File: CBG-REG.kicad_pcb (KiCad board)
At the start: 2 copper layers, 22 x 19.5 mm, 36 parts, among them J1 Conn_01x09_Socket, J2 Conn_01x09_Socket, U1 AD8560ACP-REEL7, U2 AD8560ACP-REEL7, U4 74LVC2G04

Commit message: fix: Update resistor values to those in stock at JLCPCB
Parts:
- R10, R13: value 100k -> 120k
- R11, R14: value 83.5k -> 100k
- R12: value 523k -> 634k
- R15: value 1.15M -> 1.24M
- R16: value 100k -> 107k
- R17: value 92k -> 100k
- R21: value 184k -> 178k
- R22: value 100k -> 95.3k
- R23: value 105k -> 100k
- R24: value 65.7k -> 53.6k
- R25: value 100k -> 80.6k
- R26: value 124k -> 100k
- R27: value 40.7k -> 30k
- R28: value 100k -> 75k
- R29: value 133k -> 100k
- R9: value 240k -> 287k

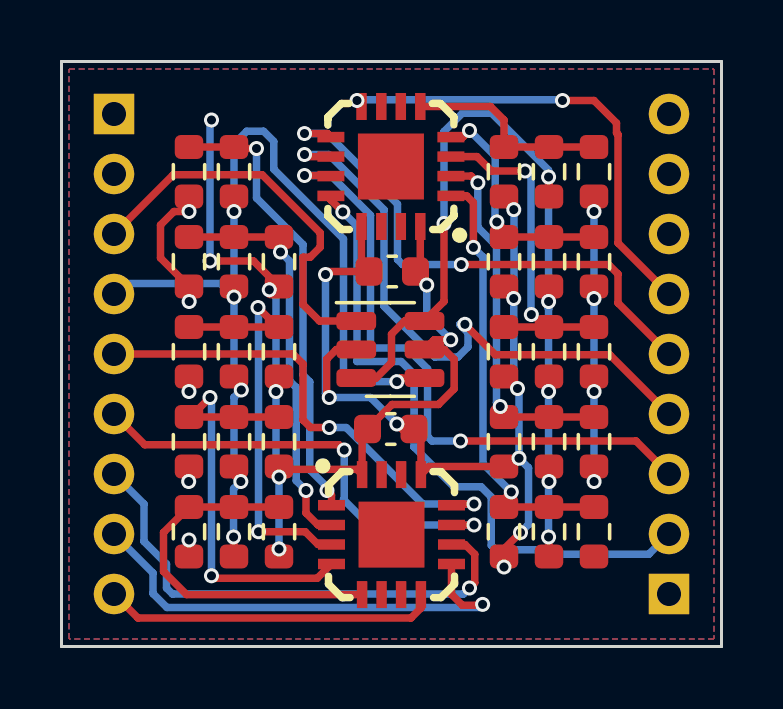
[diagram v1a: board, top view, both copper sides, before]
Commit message: feat: Add PCB silkscreen
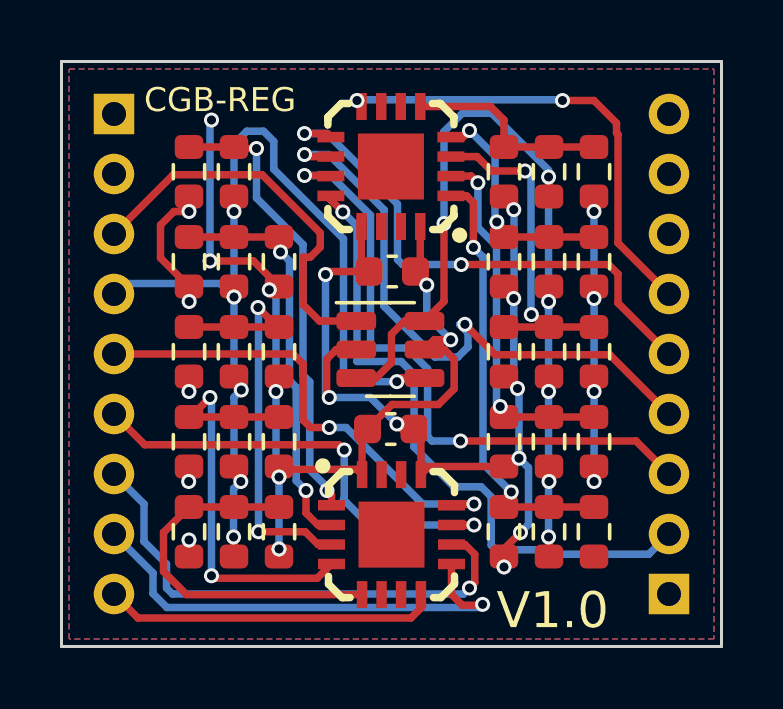
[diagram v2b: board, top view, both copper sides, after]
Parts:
- added G***: LOGO, LOGO, B.Cu at (90.0, 128.2)
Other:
- board text added: "2023"
- board text added: "Broderick Carlin"
- board text added: "CGB-REG"
- board text added: "V1.0"

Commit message: docs: Add pinout to the silkscreen
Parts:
- R17: value 100k -> 97.6k
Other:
- board text added: "Broderick"
- board text added: "COM"
- board text added: "GND"
- board text added: "NC"
- board text added: "SW"
- board text added: "V0"
- board text added: "V1"
- board text added: "V2"
- board text added: "V3"
- board text added: "V4"
- board text added: "V5"
- board text added: "V6"
- board text added: "V7"
- board text added: "V8"
- board text added: "V9"
- board text added: "VCC"
- board text removed: "Broderick Carlin"
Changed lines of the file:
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@@
     (descr "Resistor SMD 0603 (1608 Metric), square (rectangular) end terminal, IPC_7351 nominal, (Body size source: IPC-SM-782 page 72, https://www.pcb-3d.com/wordpress/wp-content/uploads/ipc-sm-782a_amendment_1_and_2.pdf), generated with kicad-footprint-generator")
     (tags "resistor")
-    (property "LCSC" "C414506")
+    (property "LCSC" "C507495")
     (property "Sheetfile" "CBG-REG.kicad_sch")
     (property "Sheetname" "")
@@
         (effects (font (size 1 1) (thickness 0.15)))
     )
-    (fp_text value "100k" (at 0 1.43 90) (layer "F.Fab") hide
+    (fp_text value "97.6k" (at 0 1.43 90) (layer "F.Fab") hide
         (effects (font (size 1 1) (thickness 0.15)))
     )
@@
   (gr_rect (start 79.25 120.75) (end 101.25 140.25)
     (stroke (width 0.1) (type default)) (fill none) (layer "Edge.Cuts"))
-  (gr_text "Broderick Carlin" (at 97.5 137.5) (layer "B.SilkS")
+  (gr_text "V7" (at 98 133.25) (layer "B.SilkS")
+    (effects (font (size 1 1) (thickness 0.15)) (justify left bottom mirror))
+  )
+  (gr_text "SW" (at 84.5 127.25) (layer "B.SilkS")
+    (effects (font (size 1 1) (thickness 0.15)) (justify left bottom mirror))
+  )
+  (gr_text "V9" (at 98 129.25) (layer "B.SilkS")
+    (effects (font (size 1 1) (thickness 0.15)) (justify left bottom mirror))
+  )
+  (gr_text "NC" (at 84.5 123.25) (layer "B.SilkS")
+    (effects (font (size 1 1) (thickness 0.15)) (justify left bottom mirror))
+  )
+  (gr_text "Broderick" (at 94.25 137.75) (layer "B.SilkS")
     (effects (font (size 1.2 1.2) (thickness 0.15)) (justify left bottom mirror))
   )
-  (gr_text "2023" (at 91.75 139.25) (layer "B.SilkS")
-    (effects (font (size 1 1) (thickness 0.15)) (justify left bottom mirror))
-  )
+  (gr_text "2023" (at 92 139.25) (layer "B.SilkS")
+    (effects (font (size 1 1) (thickness 0.15)) (justify left bottom mirror))
+  )
+  (gr_text "V0" (at 84.25 131.25) (layer "B.SilkS")
+    (effects (font (size 1 1) (thickness 0.15)) (justify left bottom mirror))
+  )
+  (gr_text "NC" (at 98 125.25) (layer "B.SilkS")
+    (effects (font (size 1 1) (thickness 0.15)) (justify left bottom mirror))
+  )
+  (gr_text "NC" (at 98 123.25) (layer "B.SilkS")
+    (effects (font (size 1 1) (thickness 0.15)) (justify left bottom mirror))
+  )
+  (gr_text "V8" (at 98 131.25) (layer "B.SilkS")
+    (effects (font (size 1 1) (thickness 0.15)) (justify left bottom mirror))
+  )
+  (gr_text "V6" (at 98 135.25) (layer "B.SilkS")
+    (effects (font (size 1 1) (thickness 0.15)) (justify left bottom mirror))
+  )
+  (gr_text "V3" (at 84.25 137.25) (layer "B.SilkS")
+    (effects (font (size 1 1) (thickness 0.15)) (justify left bottom mirror))
+  )
+  (gr_text "V2" (at 84.25 135.25) (layer "B.SilkS")
+    (effects (font (size 1 1) (thickness 0.15)) (justify left bottom mirror))
+  )
+  (gr_text "V4" (at 84.25 139.25) (layer "B.SilkS")
+    (effects (font (size 1 1) (thickness 0.15)) (justify left bottom mirror))
+  )
+  (gr_text "GND" (at 98.25 139.25) (layer "B.SilkS")
+    (effects (font (size 1 1) (thickness 0.15)) (justify left bottom mirror))
+  )
+  (gr_text "V1" (at 84.25 133.25) (layer "B.SilkS")
+    (effects (font (size 1 1) (thickness 0.15)) (justify left bottom mirror))
+  )
+  (gr_text "V5" (at 98 137.25) (layer "B.SilkS")
+    (effects (font (size 1 1) (thickness 0.15)) (justify left bottom mirror))
+  )
+  (gr_text "COM" (at 85.5 129.25) (layer "B.SilkS")
+    (effects (font (size 1 1) (thickness 0.15)) (justify left bottom mirror))
+  )
+  (gr_text "VCC" (at 98 127.25) (layer "B.SilkS")
+    (effects (font (size 1 1) (thickness 0.15)) (justify left bottom mirror))
+  )
+  (gr_text "NC" (at 84.5 125.25) (layer "B.SilkS")
+    (effects (font (size 1 1) (thickness 0.15)) (justify left bottom mirror))
+  )

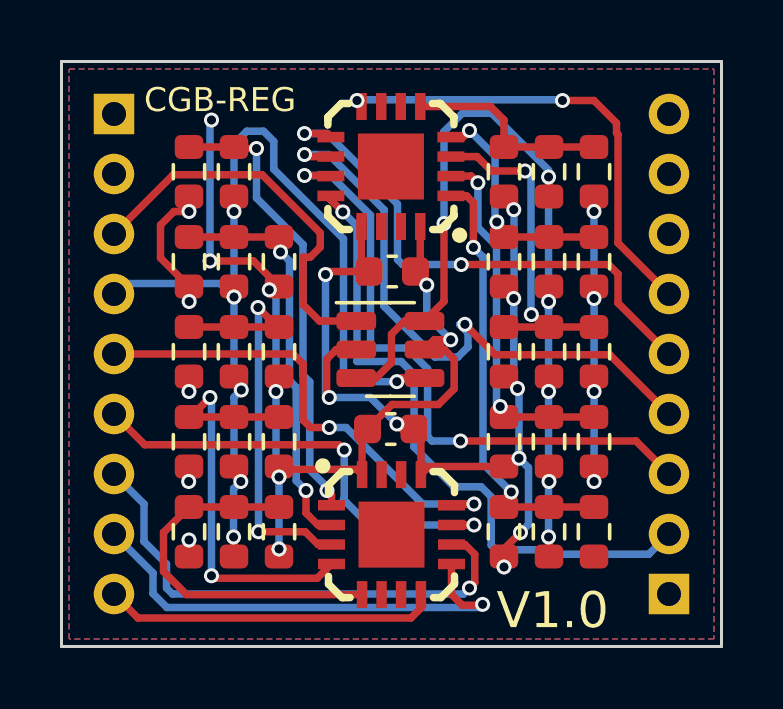
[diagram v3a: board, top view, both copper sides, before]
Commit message: feat: Switch connector to use castellations
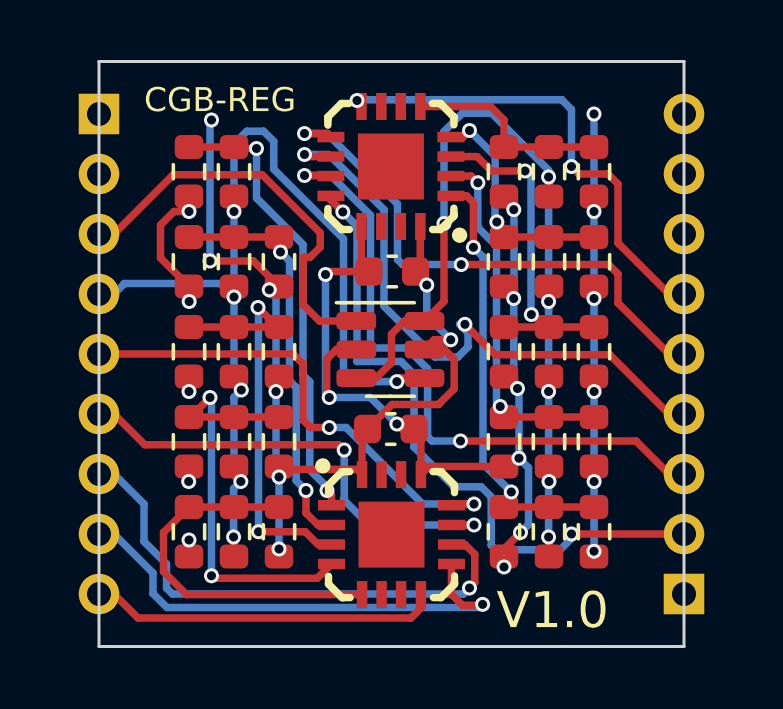
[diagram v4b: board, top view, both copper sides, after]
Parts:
- moved J1 0.50 mm to (100.0, 138.5)
- moved J2 0.50 mm to (80.5, 122.5)
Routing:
- net +5V: track 43.9 -> 49.5 mm, vias 12 -> 14
- net v5: track 21.6 -> 21.7 mm, vias 1 -> 2
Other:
- board size 22 x 19.5 mm -> 19.5 x 19.5 mm
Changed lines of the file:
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@@
   )
   (footprint "Connector_PinHeader_2.00mm:PinHeader_1x09_P2.00mm_Vertical" (layer "B.Cu")
-    (at 99.5 138.5)
+    (at 100 138.5)
     (descr "Through hole straight pin header, 1x09, 2.00mm pitch, single row")
     (tags "Through hole pin header THT 1x09 2.00mm single row")
@@
   )
   (footprint "Connector_PinHeader_2.00mm:PinHeader_1x09_P2.00mm_Vertical" (layer "B.Cu")
-    (at 81 122.5 180)
+    (at 80.5 122.5 180)
     (descr "Through hole straight pin header, 1x09, 2.00mm pitch, single row")
     (tags "Through hole pin header THT 1x09 2.00mm single row")
@@
     )
   )
-  (gr_rect (start 79.25 120.75) (end 101.25 140.25)
+  (gr_rect (start 80.5 120.75) (end 100 140.25)
     (stroke (width 0.1) (type default)) (fill none) (layer "Edge.Cuts"))
   (gr_text "V7" (at 98 133.25) (layer "B.SilkS")
@@
   (via (at 97 125.75) (size 0.5) (drill 0.3) (layers "F.Cu" "B.Cu") (net 1))
   (via (at 92.224 130.025937) (size 0.5) (drill 0.3) (layers "F.Cu" "B.Cu") (net 1))
+  (via (at 97 137.0745) (size 0.5) (drill 0.3) (layers "F.Cu" "B.Cu") (net 1))
   (via (at 84.25 122.7) (size 0.5) (drill 0.3) (layers "F.Cu" "B.Cu") (net 1))
   (via (at 97.002711 131.7505) (size 0.5) (drill 0.3) (layers "F.Cu" "B.Cu") (net 1))
@@
   (via (at 91.4255 128.2) (size 0.5) (drill 0.3) (layers "F.Cu" "B.Cu") (net 1))
   (via (at 86.175546 128.359857) (size 0.5) (drill 0.3) (layers "F.Cu" "B.Cu") (net 1))
+  (via (at 97 122.5) (size 0.5) (drill 0.3) (layers "F.Cu" "B.Cu") (net 1))
   (via (at 97 128.65) (size 0.5) (drill 0.3) (layers "F.Cu" "B.Cu") (net 1))
   (via (at 97.002711 134.7505) (size 0.5) (drill 0.3) (layers "F.Cu" "B.Cu") (net 1))
@@
   (segment (start 84.2 127.4) (end 84.2 122.75) (width 0.25) (layer "B.Cu") (net 1))
   (segment (start 97.002711 131.7505) (end 97.002711 128.652711) (width 0.25) (layer "B.Cu") (net 1))
+  (segment (start 97 125.75) (end 97 122.5) (width 0.25) (layer "B.Cu") (net 1))
   (segment (start 86.4 131.752271) (end 86.4 134.5) (width 0.25) (layer "B.Cu") (net 1))
   (segment (start 97.002711 128.652711) (end 97 128.65) (width 0.25) (layer "B.Cu") (net 1))
@@
   (segment (start 86.175546 128.359857) (end 86.4 128.584311) (width 0.25) (layer "B.Cu") (net 1))
   (segment (start 84.2 122.75) (end 84.25 122.7) (width 0.25) (layer "B.Cu") (net 1))
+  (segment (start 97.002711 137.071789) (end 97 137.0745) (width 0.25) (layer "B.Cu") (net 1))
   (segment (start 91.4255 128.2) (end 91.4255 129.227437) (width 0.25) (layer "B.Cu") (net 1))
   (segment (start 86.4 134.5) (end 86.5 134.6) (width 0.25) (layer "B.Cu") (net 1))
+  (segment (start 97.002711 134.7505) (end 97.002711 137.071789) (width 0.25) (layer "B.Cu") (net 1))
   (segment (start 86.398229 131.7505) (end 86.4 131.752271) (width 0.25) (layer "B.Cu") (net 1))
   (segment (start 86.4 128.584311) (end 86.4 131.748729) (width 0.25) (layer "B.Cu") (net 1))
@@
   (segment (start 88.23 125.368431) (end 88.626843 125.765274) (width 0.25) (layer "F.Cu") (net 3))
   (segment (start 88.23 125.23) (end 88.23 125.368431) (width 0.25) (layer "F.Cu") (net 3))
+  (segment (start 96.25 136.5) (end 99.5 136.5) (width 0.25) (layer "F.Cu") (net 3))
+  (via (at 96.25 136.5) (size 0.5) (drill 0.3) (layers "F.Cu" "B.Cu") (net 3))
   (via (at 88.626843 125.765274) (size 0.5) (drill 0.3) (layers "F.Cu" "B.Cu") (net 3))
   (segment (start 93.725 137.025) (end 95.098416 137.025) (width 0.25) (layer "B.Cu") (net 3))
   (segment (start 93.575 136.875) (end 93.725 137.025) (width 0.25) (layer "B.Cu") (net 3))
   (segment (start 93.238173 134.925497) (end 93.575 135.262324) (width 0.25) (layer "B.Cu") (net 3))
-  (segment (start 98.8255 137.1745) (end 99.5 136.5) (width 0.25) (layer "B.Cu") (net 3))
   (segment (start 95.098416 137.025) (end 95.247916 137.1745) (width 0.25) (layer "B.Cu") (net 3))
+  (segment (start 95.247916 137.1745) (end 95.724262 137.1745) (width 0.25) (layer "B.Cu") (net 3))
   (segment (start 88.626843 125.765274) (end 89.1 126.238431) (width 0.25) (layer "B.Cu") (net 3))
   (segment (start 92.325497 134.925497) (end 93.238173 134.925497) (width 0.25) (layer "B.Cu") (net 3))
+  (segment (start 95.724262 137.1745) (end 96.25 136.648762) (width 0.25) (layer "B.Cu") (net 3))
   (segment (start 91.003664 131.183129) (end 91.003664 133.596336) (width 0.25) (layer "B.Cu") (net 3))
   (segment (start 89.1 130.75) (end 90.570535 130.75) (width 0.25) (layer "B.Cu") (net 3))
   (segment (start 93.575 135.262324) (end 93.575 136.875) (width 0.25) (layer "B.Cu") (net 3))
-  (segment (start 95.247916 137.1745) (end 98.8255 137.1745) (width 0.25) (layer "B.Cu") (net 3))
+  (segment (start 96.25 136.648762) (end 96.25 136.5) (width 0.25) (layer "B.Cu") (net 3))
   (segment (start 91 133.6) (end 92.325497 134.925497) (width 0.25) (layer "B.Cu") (net 3))
   (segment (start 91.003664 133.596336) (end 91 133.6) (width 0.25) (layer "B.Cu") (net 3))
@@
   (segment (start 90.45 127.35) (end 90.45 125.502466) (width 0.25) (layer "B.Cu") (net 6))
   (segment (start 92.5745 127.519053) (end 90.619053 127.519053) (width 0.25) (layer "B.Cu") (net 6))
-  (segment (start 97 122.05) (end 97.75 122.8) (width 0.25) (layer "F.Cu") (net 7))
-  (segment (start 95.95 122.05) (end 97 122.05) (width 0.25) (layer "F.Cu") (net 7))
-  (segment (start 97.8 123.182538) (end 97.8 126.8) (width 0.25) (layer "F.Cu") (net 7))
-  (segment (start 97.75 123.132538) (end 97.8 123.182538) (width 0.25) (layer "F.Cu") (net 7))
+  (segment (start 96.5 124.5) (end 96.25 124.25) (width 0.25) (layer "F.Cu") (net 7))
+  (segment (start 97.467462 124.5) (end 96.5 124.5) (width 0.25) (layer "F.Cu") (net 7))
+  (segment (start 97.8 124.832538) (end 97.467462 124.5) (width 0.25) (layer "F.Cu") (net 7))
+  (segment (start 97.8 126.8) (end 97.8 124.832538) (width 0.25) (layer "F.Cu") (net 7))
   (segment (start 89.25 122.2) (end 89.25 122.25) (width 0.25) (layer "F.Cu") (net 7))
-  (segment (start 97.75 122.8) (end 97.75 123.132538) (width 0.25) (layer "F.Cu") (net 7))
   (segment (start 97.8 126.8) (end 99.5 128.5) (width 0.25) (layer "F.Cu") (net 7))
   (segment (start 89.1 122.05) (end 89.25 122.2) (width 0.25) (layer "F.Cu") (net 7))
-  (via (at 95.95 122.05) (size 0.5) (drill 0.3) (layers "F.Cu" "B.Cu") (net 7))
+  (via (at 96.25 124.25) (size 0.5) (drill 0.3) (layers "F.Cu" "B.Cu") (net 7))
   (via (at 89.1 122.05) (size 0.5) (drill 0.3) (layers "F.Cu" "B.Cu") (net 7))
-  (segment (start 95.925 122.025) (end 95.95 122.05) (width 0.25) (layer "B.Cu") (net 7))
-  (segment (start 89.125 122.025) (end 95.925 122.025) (width 0.25) (layer "B.Cu") (net 7))
-  (segment (start 89.1 122.05) (end 89.125 122.025) (width 0.25) (layer "B.Cu") (net 7))
+  (segment (start 89.125 122.025) (end 89.1 122.05) (width 0.25) (layer "B.Cu") (net 7))
+  (segment (start 96.25 122.35) (end 95.925 122.025) (width 0.25) (layer "B.Cu") (net 7))
+  (segment (start 95.925 122.025) (end 89.125 122.025) (width 0.25) (layer "B.Cu") (net 7))
+  (segment (start 96.25 124.25) (end 96.25 122.35) (width 0.25) (layer "B.Cu") (net 7))
   (segment (start 87.3 128.85) (end 87.85 129.4) (width 0.25) (layer "F.Cu") (net 12))
   (segment (start 87.875 126.461827) (end 87.875 126.938173) (width 0.25) (layer "F.Cu") (net 12))
@@
     (polygon
       (pts
-        (xy 79.5 121)
-        (xy 101 121)
-        (xy 101 140)
-        (xy 79.5 140)
+        (xy 80.5 120.75)
+        (xy 100 120.75)
+        (xy 100 140.25)
+        (xy 80.5 140.25)
       )
     )
@@
     (polygon
       (pts
-        (xy 79.5 121)
-        (xy 101 121)
-        (xy 101 140)
-        (xy 79.5 140)
+        (xy 80.5 120.75)
+        (xy 100 120.75)
+        (xy 100 140.25)
+        (xy 80.5 140.25)
       )
     )

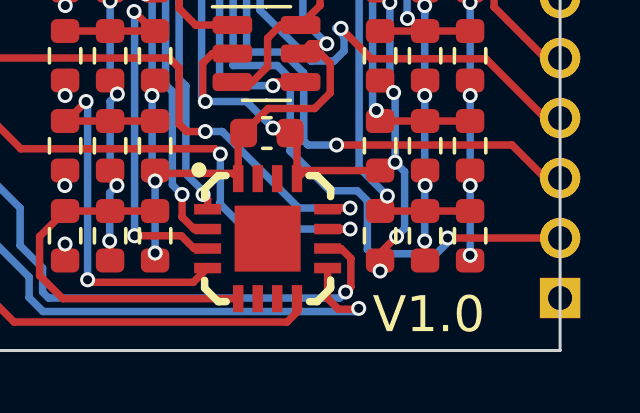
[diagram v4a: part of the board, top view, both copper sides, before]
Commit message: feat: Bump schematic version to v1.1
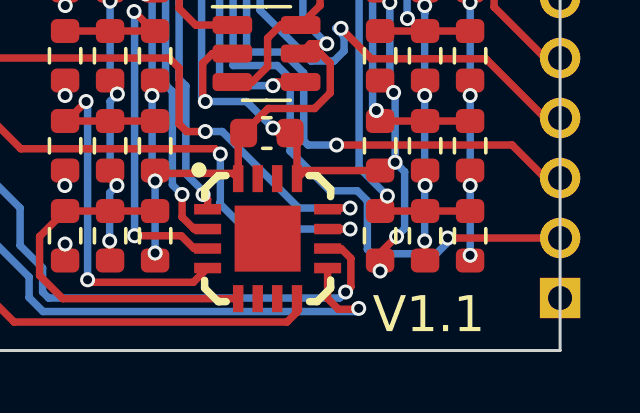
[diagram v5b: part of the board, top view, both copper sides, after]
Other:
- board text added: "V1.1"
- board text removed: "V1.0"
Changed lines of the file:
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@@
     (effects (font (size 1 1) (thickness 0.15)) (justify left bottom mirror))
   )
-  (gr_text "V1.0" (at 93.75 139.75) (layer "F.SilkS")
+  (gr_text "V1.1" (at 93.75 139.75) (layer "F.SilkS")
     (effects (font (size 1.2 1.2) (thickness 0.15)) (justify left bottom))
   )
